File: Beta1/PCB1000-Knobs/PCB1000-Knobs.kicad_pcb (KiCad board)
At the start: 2 copper layers, 188.9 x 30.9 mm, 39 parts, among them U1000 MCP3008T-I/SL, U2 MCP3008T-I/SL

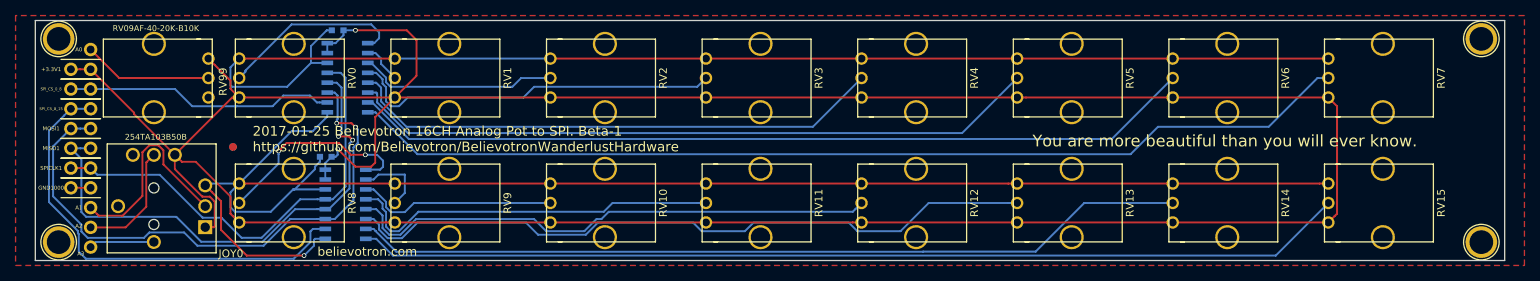
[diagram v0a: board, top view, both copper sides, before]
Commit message: Moved. Renamed. Added "PCB1000-KNOBS" to PCB silk
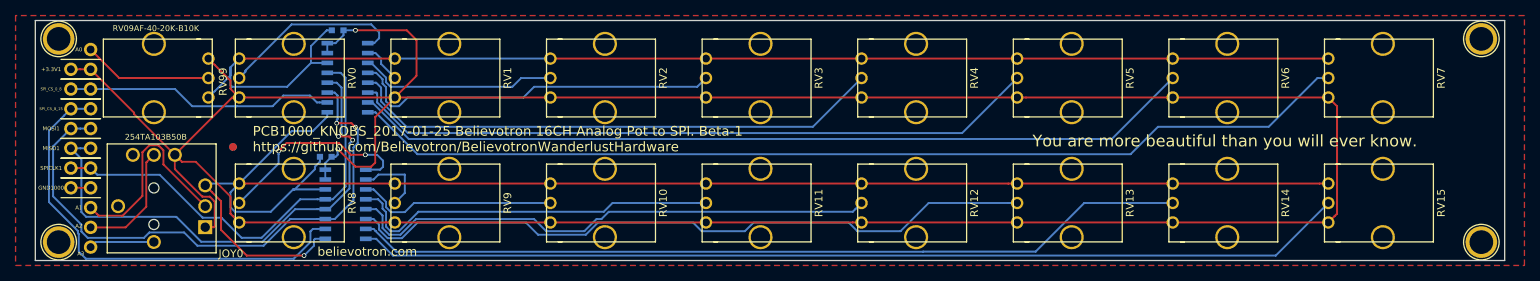
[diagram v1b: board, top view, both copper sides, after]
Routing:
- net GND: track 372.7 -> 377.8 mm
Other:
- board text added: "PCB1000_KNOBS_2017-01-25 Believotron 16CH Analog Pot to SPI. Beta-1 https://github.com/Believotron/BelievotronWanderlustHardware"
- board text removed: "2017-01-25 Believotron 16CH Analog Pot to SPI. Beta-1 https://github.com/Believotron/BelievotronWanderlustHardware"
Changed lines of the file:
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@@
   (general
     (links 86)
-    (no_connects 1)
-    (area 2.489999 -31.537501 191.470001 -0.587499)
+    (no_connects 0)
+    (area 0 -33.148 193.960001 1.255473)
     (thickness 1.6)
     (drawings 20)
-    (tracks 388)
+    (tracks 391)
     (zones 0)
     (modules 39)
@@
     (effects (font (size 1.5 1.5) (thickness 0.3)) (justify mirror))
   )
-  (gr_text believotron.com (at 45.212 -1.778 360) (layer F.SilkS)
+  (gr_text believotron.com (at 45.212 -1.778) (layer F.SilkS)
     (effects (font (size 1.15 1.15) (thickness 0.2875)))
   )
@@
     (effects (font (size 1.5 1.5) (thickness 0.3)))
   )
-  (gr_text "2017-01-25 Believotron 16CH Analog Pot to SPI. Beta-1\nhttps://github.com/Believotron/BelievotronWanderlustHardware\n" (at 30.48 -16.256) (layer F.SilkS)
+  (gr_text "PCB1000_KNOBS_2017-01-25 Believotron 16CH Analog Pot to SPI. Beta-1\nhttps://github.com/Believotron/BelievotronWanderlustHardware\n" (at 30.48 -16.256) (layer F.SilkS)
     (effects (font (size 1.25 1.25) (thickness 0.25)) (justify left))
   )
@@
   (gr_line (start 2.54 -0.6375) (end 2.54 -31.4875) (layer Edge.Cuts) (width 0.1))
   (gr_line (start 2.54 -0.6375) (end 191.42 -0.6375) (layer Edge.Cuts) (width 0.1))
+  (segment (start 28.7496 -26.594) (end 27.624599 -25.468999) (width 0.25) (layer B.Cu) (net 1))
+  (segment (start 27.624599 -25.468999) (end 27.624599 -24.428199) (width 0.25) (layer B.Cu) (net 1))
+  (segment (start 27.624599 -24.428199) (end 25.590399 -22.393999) (width 0.25) (layer B.Cu) (net 1))
+  (segment (start 25.590399 -22.393999) (end 24.7904 -21.594) (width 0.25) (layer B.Cu) (net 1))
   (segment (start 14.5426 -14.7574) (end 15.08 -14.22) (width 0.25) (layer F.Cu) (net 1))
   (segment (start 48.7496 -26.594) (end 68.7496 -26.594) (width 0.25) (layer B.Cu) (net 1))
@@
   (segment (start 27.624599 -23.175401) (end 27.831001 -22.968999) (width 0.25) (layer B.Cu) (net 1))
   (segment (start 27.831001 -22.968999) (end 34.906999 -22.968999) (width 0.25) (layer B.Cu) (net 1))
-  (segment (start 28.7496 -26.594) (end 27.624599 -25.468999) (width 0.25) (layer B.Cu) (net 1))
   (segment (start 27.624599 -25.468999) (end 27.624599 -23.175401) (width 0.25) (layer B.Cu) (net 1))
   (segment (start 9.649605 -9.979527) (end 8.428291 -9.979527) (width 0.25) (layer F.Cu) (net 1))
